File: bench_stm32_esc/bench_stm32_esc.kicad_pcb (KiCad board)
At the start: 4 copper layers, 117 x 75 mm, 107 parts, among them CN1 S6B-PH-K-S-, CN10 Conn_02x19_Odd_Even, CN7 Conn_02x19_Odd_Even, J1 XT60PW-M, Q1 CSD19532Q5B, Q2 CSD19532Q5B, Q3 CSD19532Q5B, Q4 CSD19532Q5B, Q5 CSD19532Q5B, Q6 CSD19532Q5B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

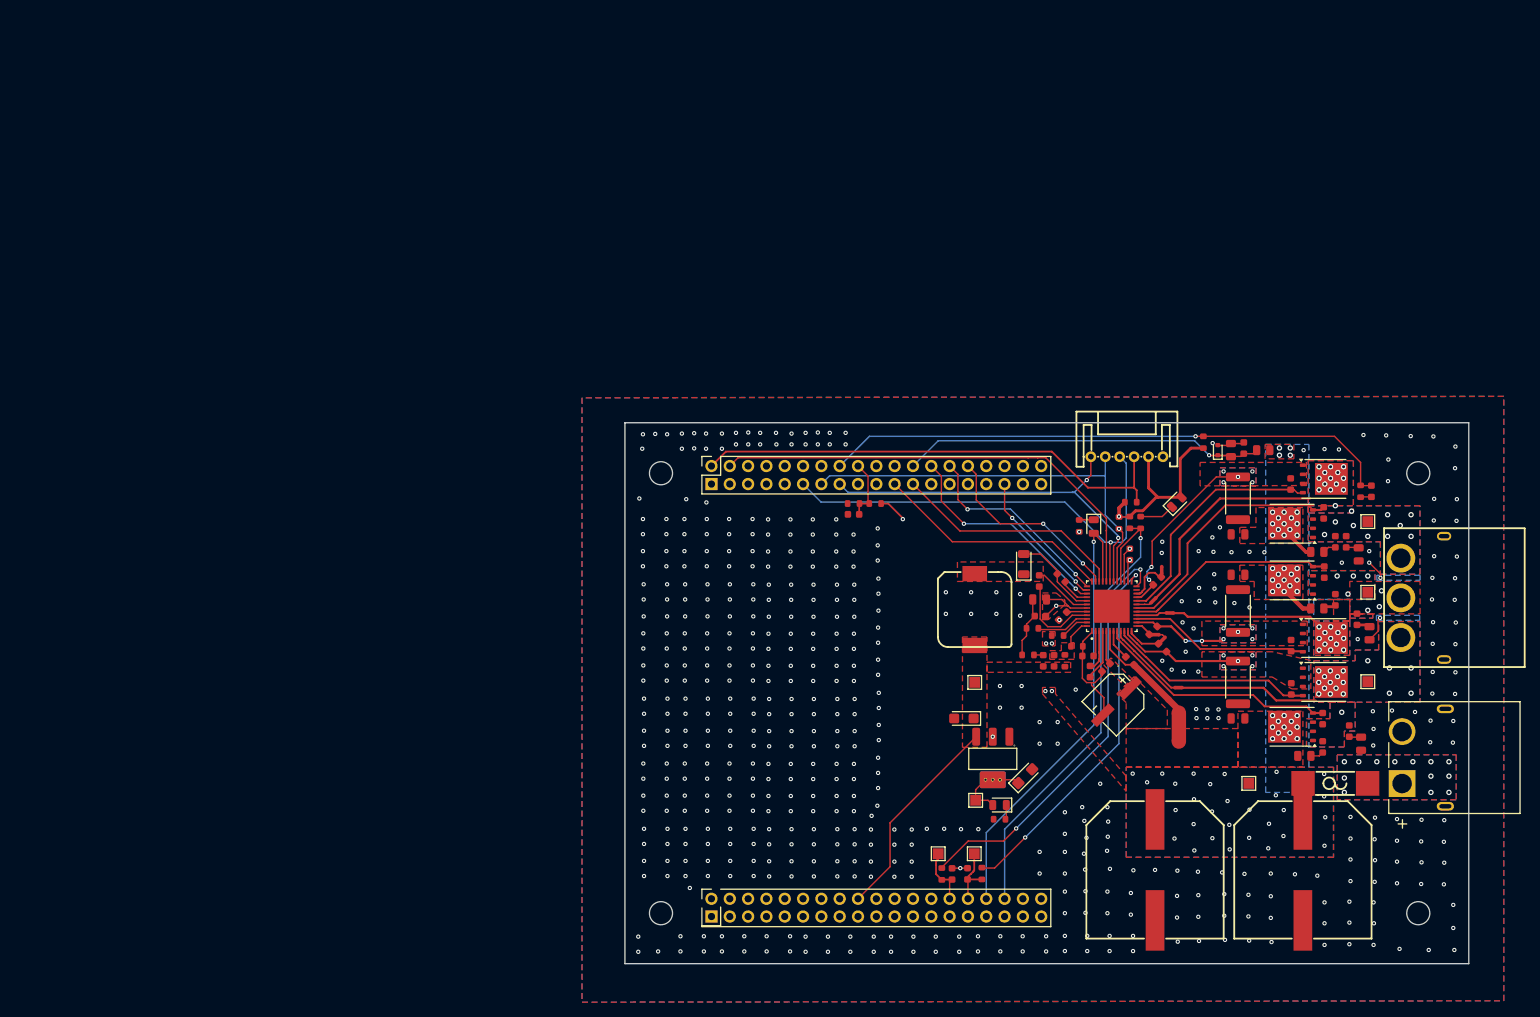
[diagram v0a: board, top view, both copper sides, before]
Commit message: Fixed 5V input to NUCLEO Board
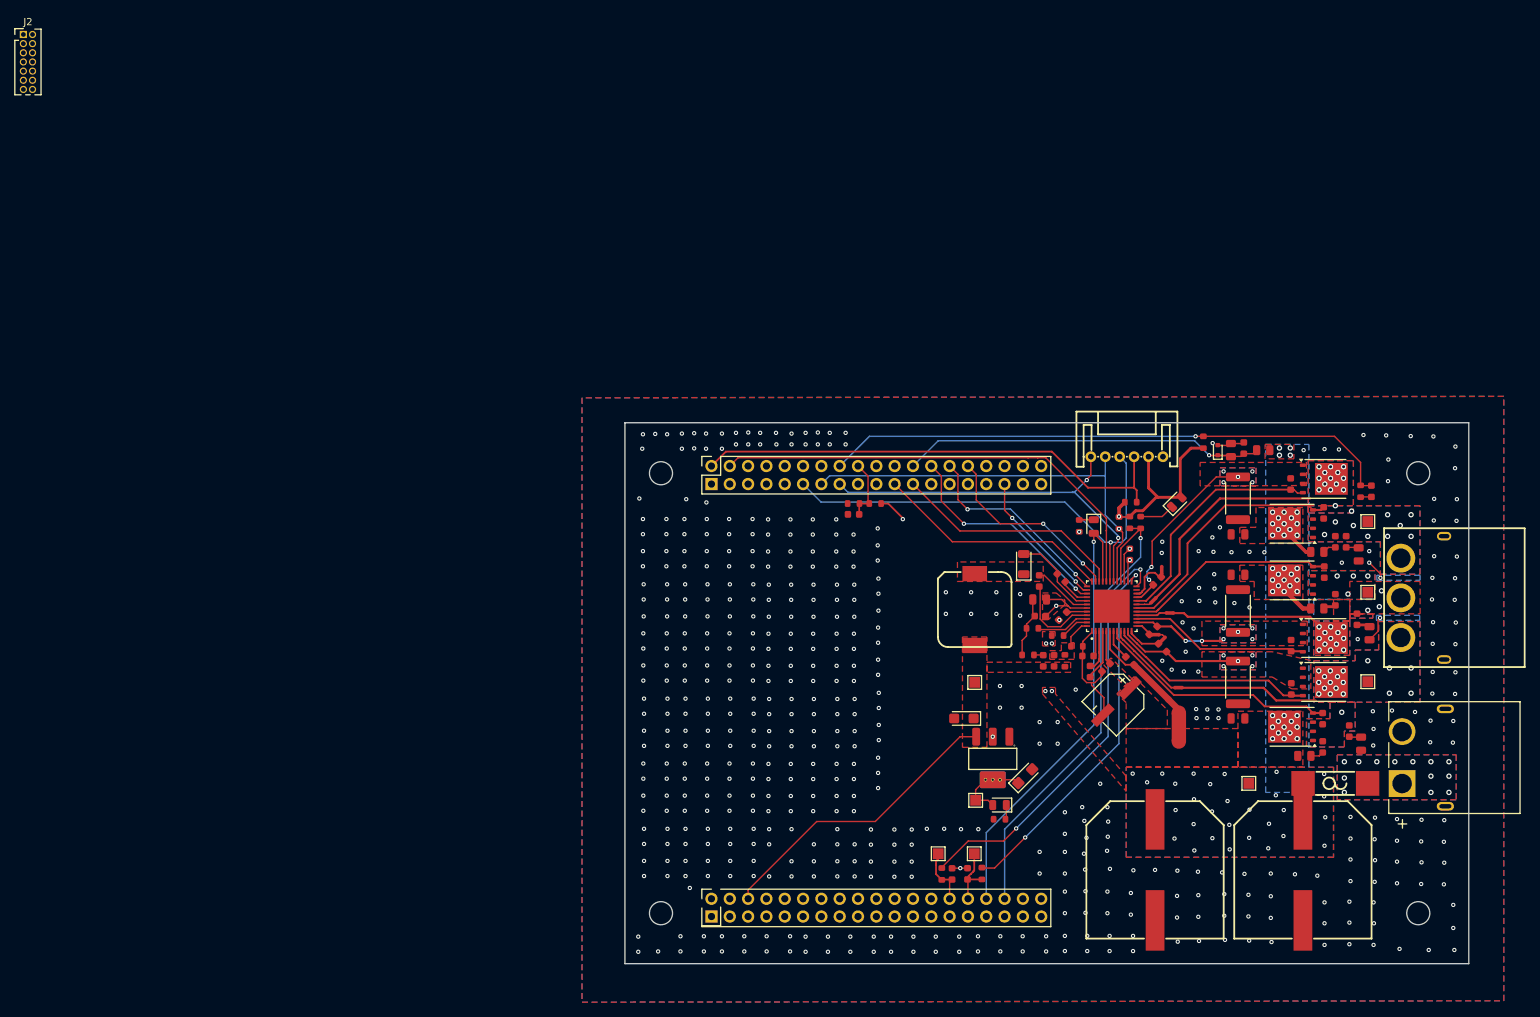
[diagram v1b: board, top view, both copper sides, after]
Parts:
- added J2: Conn_ST_STDC14, Connector_PinHeader_1.27mm:PinHeader_2x07_P1.27mm_Vertical, F.Cu at (1.59, 1.17)
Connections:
- CN7 pad 18: VBUCK -> unconnected-(CN7-Pin_18-Pad18)
- CN7 pad 6: unconnected-(CN7-Pin_6-Pad6) -> VBUCK
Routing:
- net VBUCK: track 29.3 -> 41.6 mm
- net GND: vias 547 -> 541
